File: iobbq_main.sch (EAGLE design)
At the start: 98 parts, among them K1 SRD-5VDC-SL-C, K2 SRD-5VDC-SL-C, X1 JST-XH-5-B5B-XH-A, X10 MPT0.5/8-2.54, X11 PIIKKIRIMA-7, X12 TE_RUUVULIITIN2, X13 TE_RUUVILIITIN2, X14 TE_RUUVILIITIN2, X16 TE_RUUVILIITIN3, X2 MPT0.5/8-2.54, X3 JST-XH-5-B5B-XH-A, X4 MPT0.5/8-2.54, X5 MPT0.5/8-2.54, X6 MPT0.5/8-2.54, X7 MPT0.5/8-2.54, X8 PIIKKIRIMA-4, X9 PIIKKIRIMA-7

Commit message: update values
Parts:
- added U$3: DAFUG, dafug:DAFUG
- C1, C12, C2, C26, C3: value CAP0603 -> 100n
- C10, C11: value CAP0805 -> 10µ 16V
- C13, C24, C25, C4, C5, C6, C7, C8, C9: value CAP0805 -> 1µ 16V
- C18: value CAP0805 -> 10n
- C19, C20: value CAP0603 -> NA
- C21, C22: value CAP0805 -> 2µ2 50V
- D1, D9: value (none) -> STPS340U
- N2: value LD117AS33TR -> AZ1117EH-3.3
- OK1, OK2, OK3, OK4, OK5, OK6: value SFH6186-2 -> EL817SC
- R1: value RES0603 -> 402R 0.1%
- R10, R11, R12, R13, R14, R15, R16, R17, R18, R19, R2, R20, R21, R22, R23, R24, R25, R26, R27, R28, R39, R43, R44, R45, R9: value RES0603 -> 3k24
- R3, R4, R5, R6, R7, R8: value RES0805 -> 1k21
- R38: value RES0603 -> 10k0
- R40: value RES0603 -> NA
- X12: value TE_RUUVULIITIN2 -> TE 282837-2; device OMAT_IC:TE_RUUVULIITIN2 -> OMAT_IC:TE_RUUVILIITIN2
- X13, X14: value TE_RUUVILIITIN2 -> TE 282837-2
- X16: value TE_RUUVILIITIN3 -> TE 282837-3
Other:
- note added: "3mA @ 5V"
- note added: "9mA @ 12V"
- note added: "BARBEQUE CONTROLLER KIMMOLI 2015"
- note added: "~18.2 mV/LSB Max range 18.6V"
- moved on the sheet: R41, R42

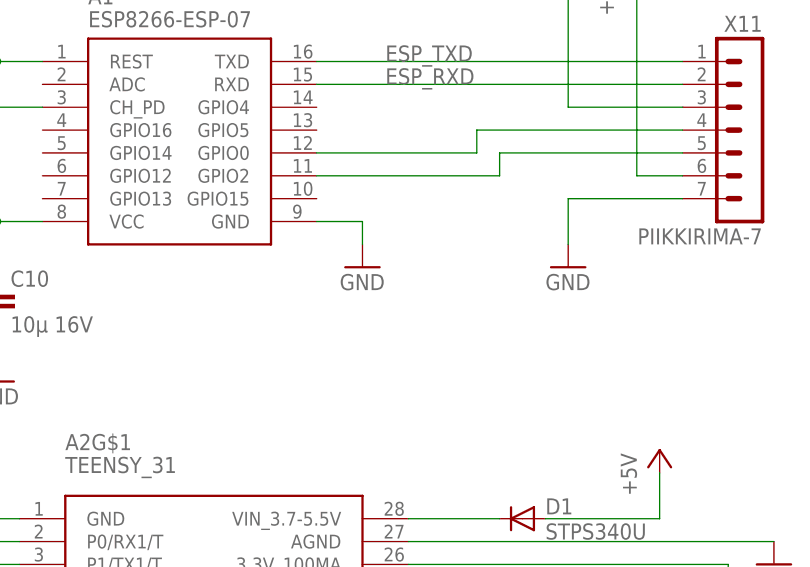
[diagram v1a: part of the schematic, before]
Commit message: pull ESP8266 GPIO15 down
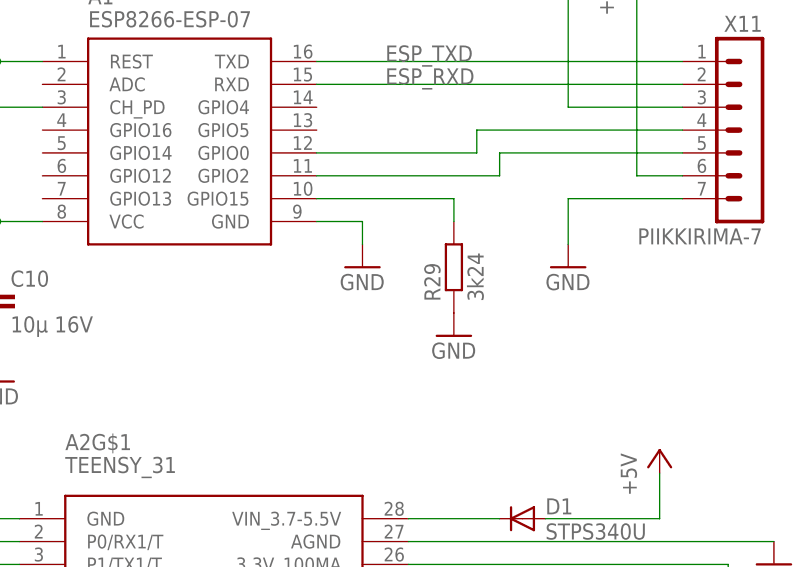
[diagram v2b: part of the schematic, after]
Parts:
- added R29: 3k24, OMAT_IC:RES0603
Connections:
- new net N$17: A1.GPIO15, R29.2
- net GND: now also R29.1
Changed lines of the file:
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@@
 <part name="X16" library="OMAT_IC" deviceset="TE_RUUVILIITIN3" device="" value="TE 282837-3"/>
 <part name="U$3" library="dafug" deviceset="DAFUG" device=""/>
+<part name="R29" library="OMAT_IC" deviceset="RES" device="0603" value="3k24"/>
+<part name="GND34" library="EKE" deviceset="GND" device=""/>
 </parts>
 <sheets>
@@
 <instance part="X16" gate="G$1" x="-27.94" y="474.98"/>
 <instance part="U$3" gate="G$1" x="25.4" y="66.04"/>
+<instance part="R29" gate="G$1" x="121.92" y="195.58" rot="R90"/>
+<instance part="GND34" gate="1" x="121.92" y="187.96"/>
 </instances>
 <busses>
@@
 <pinref part="X16" gate="G$1" pin="2"/>
 </segment>
+<segment>
+<pinref part="R29" gate="G$1" pin="1"/>
+<pinref part="GND34" gate="1" pin="GND"/>
+</segment>
 </net>
 <net name="+5V" class="0">
@@
 </segment>
 </net>
+<net name="N$17" class="0">
+<segment>
+<pinref part="R29" gate="G$1" pin="2"/>
+<wire x1="121.92" y1="200.66" x2="121.92" y2="203.2" width="0.1524" layer="91"/>
+<pinref part="A1" gate="G$1" pin="GPIO15"/>
+<wire x1="121.92" y1="203.2" x2="106.68" y2="203.2" width="0.1524" layer="91"/>
+</segment>
+</net>
